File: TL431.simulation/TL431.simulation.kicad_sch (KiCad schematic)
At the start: 0 parts

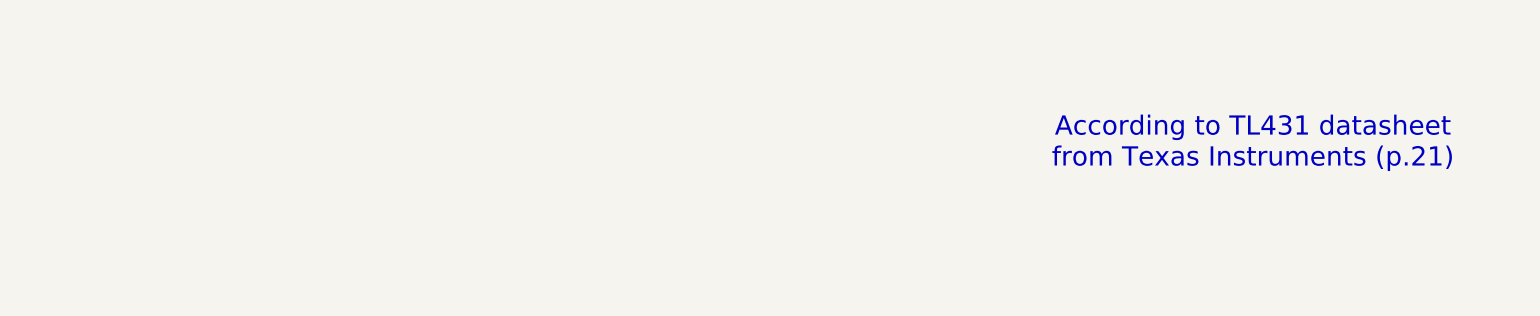
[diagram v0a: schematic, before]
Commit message: Implement TL431 model and simulation
* Implement TL431 model according to Texas Instruments datasheet.
* Implement example test from datasheet where Vka  > Vref.
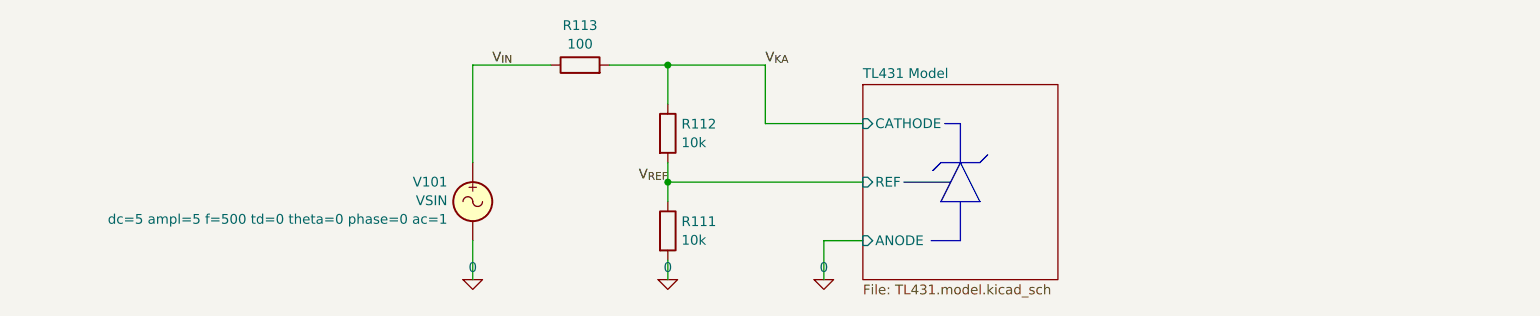
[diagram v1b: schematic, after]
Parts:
- added R111, R112: 10k, symbol Device:R
- added R113: 100, symbol Device:R
- added V101: VSIN, symbol Simulation_SPICE:VSIN
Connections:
- new net 0: R111.2, V101.2
- new net V_{IN}: R113.1, V101.1
- new net V_{KA}: R112.1, R113.2
- new net V_{REF}: R111.1, R112.2
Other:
- added sheet TL431 Model (TL431.model.kicad_sch)
- note removed: "According to TL431 datasheet from Texas Instruments (p.21)"

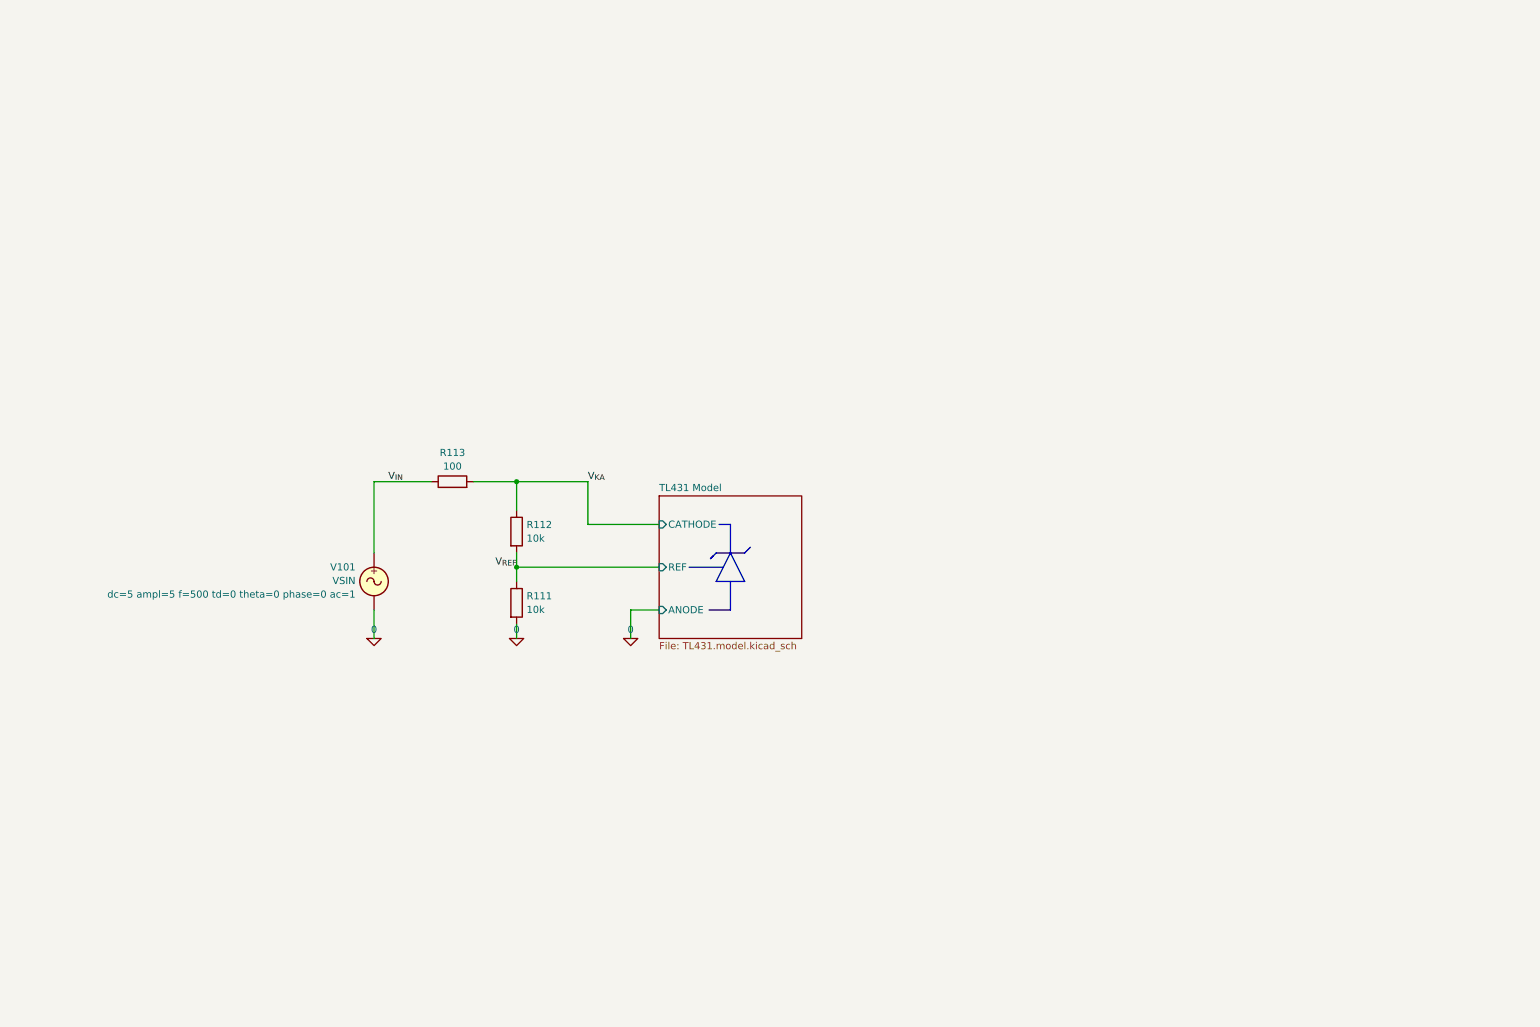
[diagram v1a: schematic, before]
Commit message: Add AS431 model to simulation for comparison
* Create local library to host TL431 symbol linked to simulation model.
* Use AS431 from Diodes Inc. as simulation model for TL431
* Add some little update/modifs/fix to simulation model since the
  simulator complains about a syntax error :
  ```
      Error on line 24 or its substitute:
      .nodeset r3_n 1
      Error: .nodeset syntax error.
      Error: circuit not parsed.
  ```
  This is documented within the model in case I understand what's wrong
  and find an actual way to fix it instead of the current workaround.
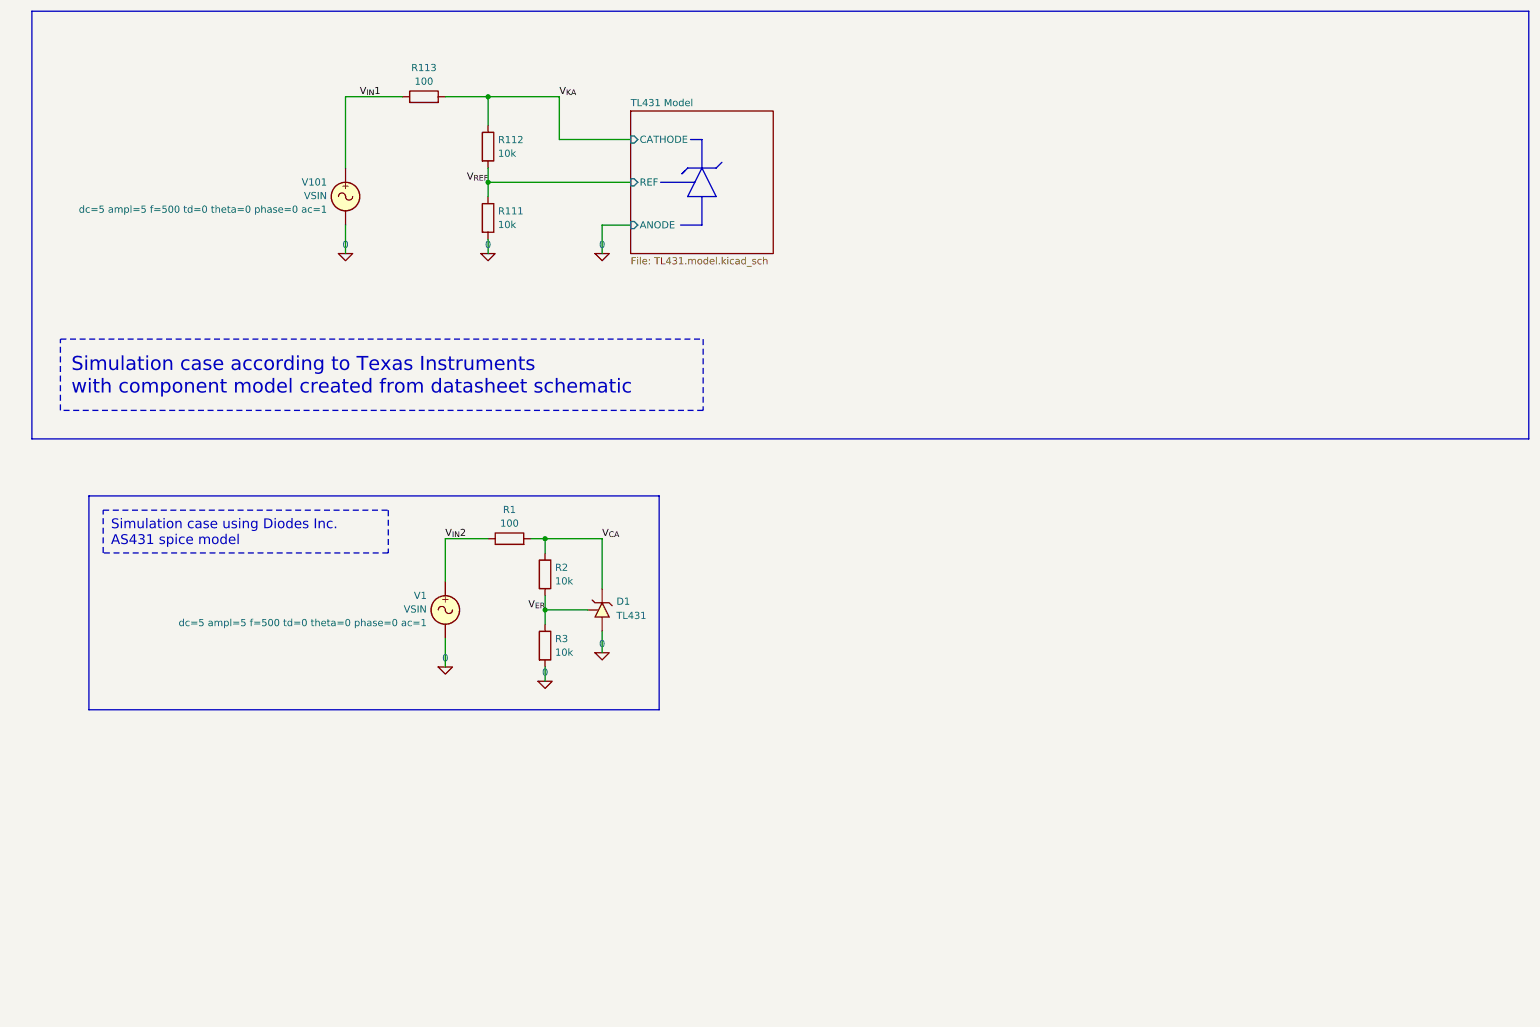
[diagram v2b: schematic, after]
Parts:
- added D1: TL431, symbol TL431.simulation_model:TL431
- added R1: 100, symbol Device:R
- added R2, R3: 10k, symbol Device:R
- added V1: VSIN, symbol Simulation_SPICE:VSIN
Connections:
- net 0: now also D1.A (ANODE), R3.2, V1.2
- net V_{IN} renamed V_{IN}1
- new net V_{CA}: D1.K (CATHODE), R1.2, R2.1
- new net V_{ER}: D1.R (REF), R2.2, R3.1
- new net V_{IN}2: R1.1, V1.1
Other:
- moved on the sheet: R111, R112, R113, V101

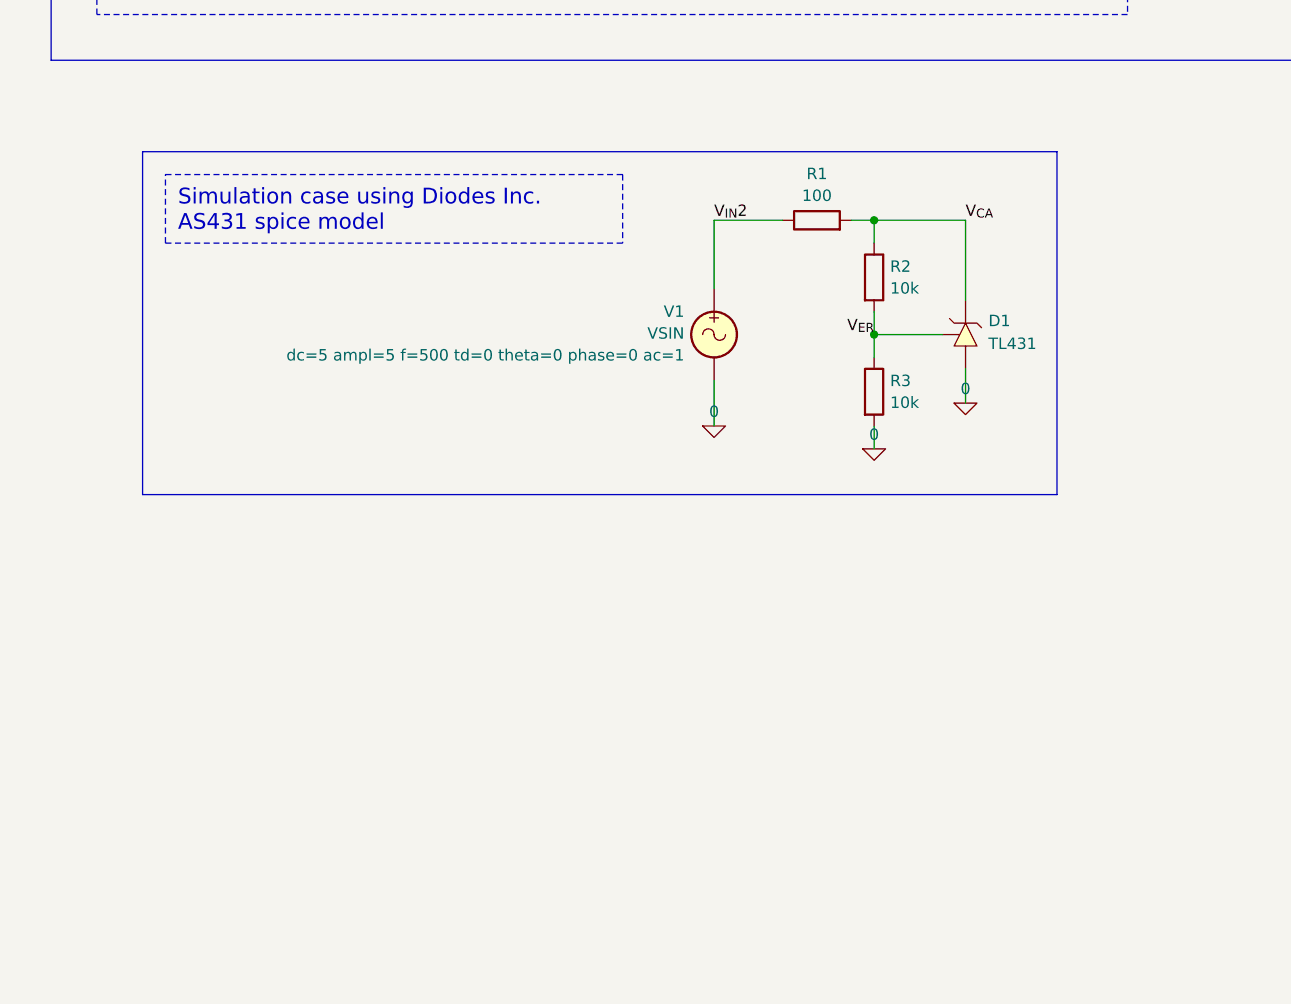
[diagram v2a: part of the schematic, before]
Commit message: Add SFH6156 photocoupler model and test
* Create dedicated symbol library for SFH6156-2 photocoupler
* Import model from Vishay and link it to symbol. I don't understand
  why it was not working initially but copy pasting the text to a new
  file solved the issue.
* Implement test from Diode Inc. datasheet to try test symbols and models.
  This is not very conclusive at this point but with another model it
  photocoupler model we might confirm that the whole thing is working.
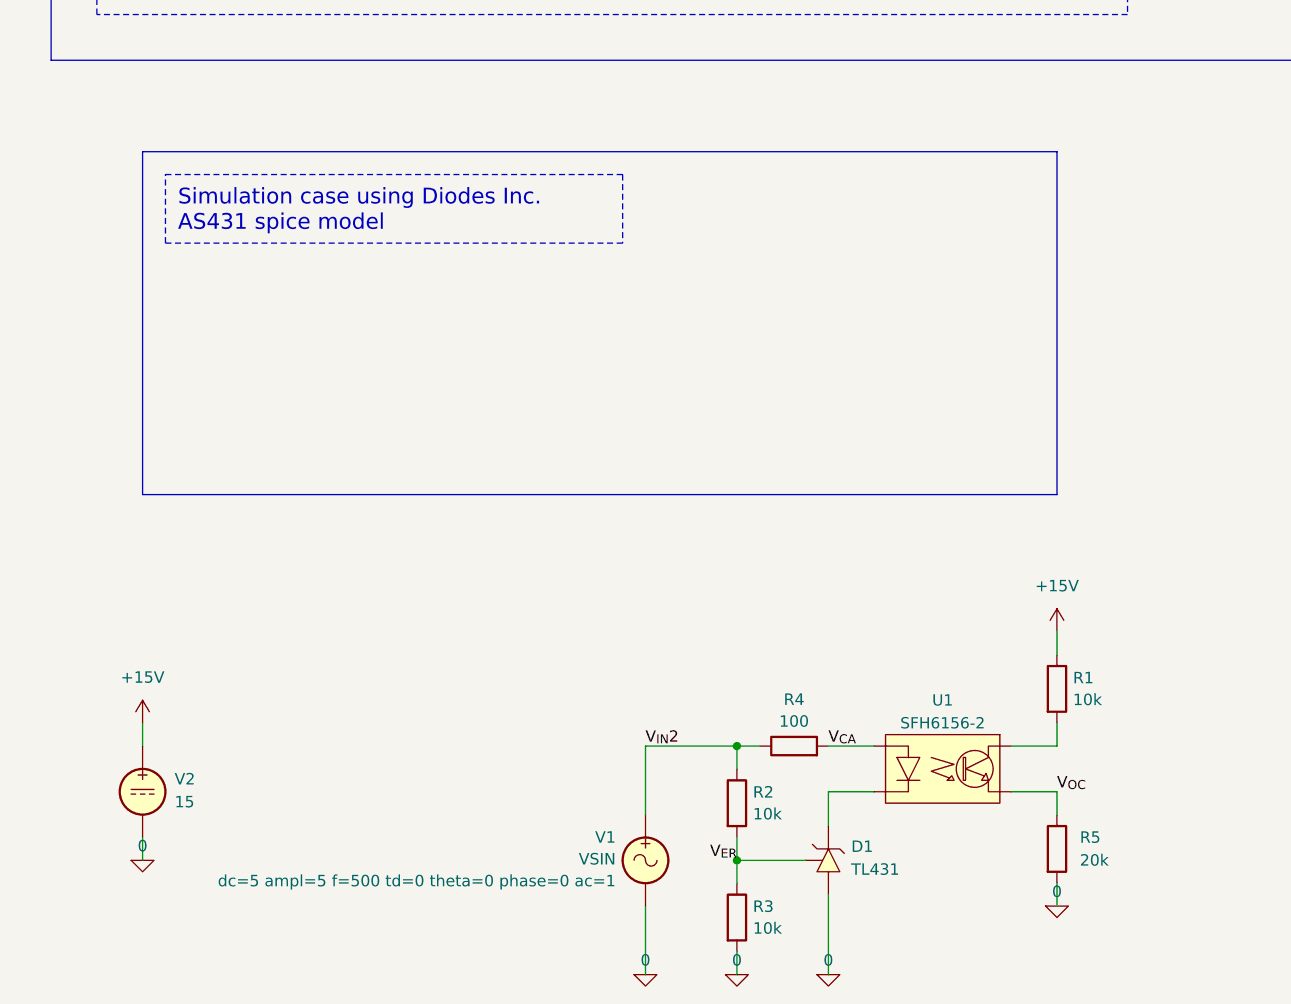
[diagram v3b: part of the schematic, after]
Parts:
- added R4: 100, symbol Device:R
- added R5: 20k, symbol Device:R
- added U1: SFH6156-2, symbol SFH6156-2.simulation_model:SFH6156-2
- added V2: 15, symbol Simulation_SPICE:VDC
- R1: value 100 -> 10k
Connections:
- net 0: now also R5.2, V2.2
- net V_{CA}: now also R4.2, U1.A (ANODE); no longer D1.K (CATHODE), R1.2, R2.1
- net V_{IN}2: now also R2.1, R4.1; no longer R1.1
- new net: D1.K (CATHODE), U1.K (CATHODE)
- new net: R1.2, U1.C (COLLECTOR)
- new net +15V: R1.1, V2.1
- new net V_{OC}: R5.1, U1.E (EMITTER)
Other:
- moved on the sheet: D1, R2, R3, V1

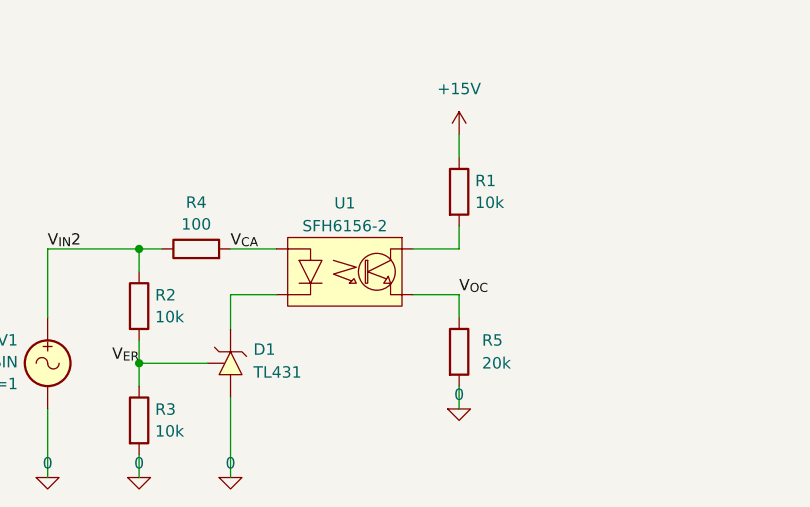
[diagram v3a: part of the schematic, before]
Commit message: Update simulation with new photocoupler
* Remove PCB file from project since it is not used
* Make use of PS2561F-1 optocoupler instead of SFH6156-2
* Fix first line in simulation model file : apparently it is ignored in most SPICE implementation but not in KiCad.
* Update photocoupler symbol with more accurate informations and datasheet.
* Rerun simulation : it looks like something works now we have to understand why the signal is so small.
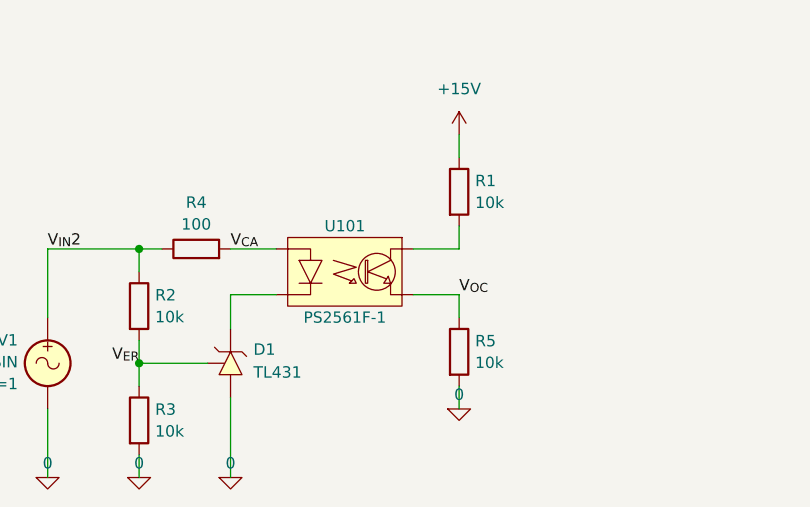
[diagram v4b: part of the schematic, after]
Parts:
- removed U1: SFH6156-2, symbol SFH6156-2.simulation_model:SFH6156-2
- added U101: PS2561F-1, symbol SFH6156-2.simulation_model:PS2561F-1
- R5: value 20k -> 10k
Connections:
- net V_{CA}: now also U101.A (ANODE)
- net V_{OC}: now also U101.E (EMITTER)
- net at D1.K (CATHODE): now also U101.K (CATHODE)
- net at R1.2: now also U101.C (COLLECTOR)
